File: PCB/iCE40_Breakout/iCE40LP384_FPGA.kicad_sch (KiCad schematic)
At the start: 31 parts, among them J1 Conn_01x08, J2 Conn_01x10, J3 Conn_01x10, Q1 L2N7002SLLT1G, SW1 KH-6X6X5H-STM, U1 ICE40LP384-SG32

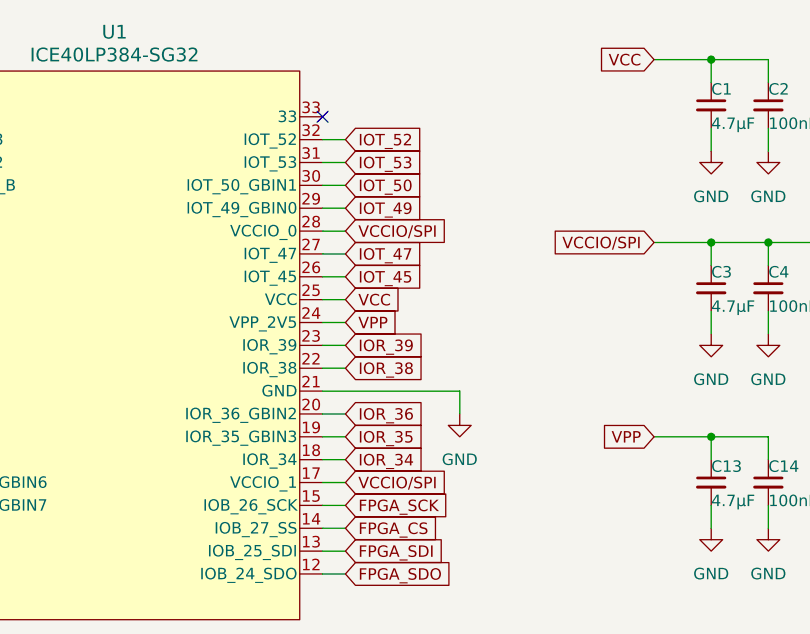
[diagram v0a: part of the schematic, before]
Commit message: Attached thermal pad to ground
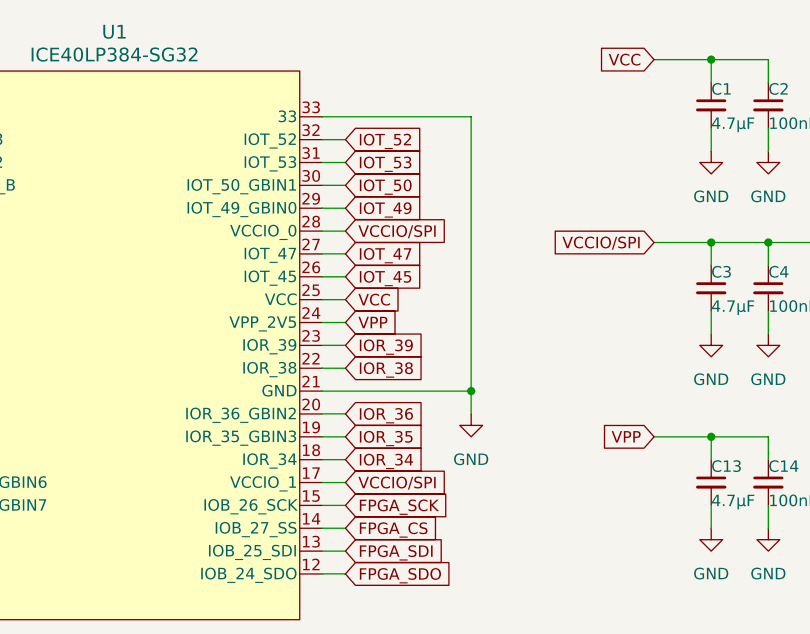
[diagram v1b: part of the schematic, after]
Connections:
- net GND: now also U1.33
- no-connect marks 1 -> 0
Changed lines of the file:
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@@
 	)
 	(junction
+		(at 123.19 60.96)
+		(diameter 0)
+		(color 0 0 0 0)
+	)
+	(junction
 		(at 215.9 44.45)
 		(diameter 0)
@@
 		(color 0 0 0 0)
 	)
-	(no_connect
-		(at 106.68 30.48)
-	)
 	(wire
 		(pts
@@
 	(wire
 		(pts
-			(xy 106.68 60.96) (xy 121.92 60.96)
+			(xy 106.68 60.96) (xy 123.19 60.96)
 		)
 		(stroke
@@
 	(wire
 		(pts
+			(xy 123.19 30.48) (xy 123.19 60.96)
+		)
+		(stroke
+			(width 0)
+			(type default)
+		)
+	)
+	(wire
+		(pts
 			(xy 248.92 143.51) (xy 255.27 143.51)
 		)
@@
 	(wire
 		(pts
-			(xy 121.92 60.96) (xy 121.92 63.5)
+			(xy 123.19 60.96) (xy 123.19 63.5)
 		)
 		(stroke
@@
 	(wire
 		(pts
+			(xy 106.68 30.48) (xy 123.19 30.48)
+		)
+		(stroke
+			(width 0)
+			(type default)
+		)
+	)
+	(wire
+		(pts
 			(xy 30.48 133.35) (xy 30.48 135.89)
 		)
@@
 	(symbol
 		(lib_id "power:GND")
-		(at 121.92 63.5 0)
+		(at 123.19 63.5 0)
 		(unit 1)
 		(exclude_from_sim no)
@@
 		(fields_autoplaced yes)
 		(property "Reference" "#PWR014"
-			(at 121.92 69.85 0)
+			(at 123.19 69.85 0)
 			(effects
 				(font
@@
 		)
 		(property "Value" "GND"
-			(at 121.92 68.58 0)
+			(at 123.19 68.58 0)
 			(effects
 				(font
@@
 		)
 		(property "Footprint" ""
-			(at 121.92 63.5 0)
+			(at 123.19 63.5 0)
 			(effects
 				(font
@@
 		)
 		(property "Datasheet" ""
-			(at 121.92 63.5 0)
+			(at 123.19 63.5 0)
 			(effects
 				(font
@@
 		)
 		(property "Description" "Power symbol creates a global label with name \"GND\" , ground"
-			(at 121.92 63.5 0)
+			(at 123.19 63.5 0)
 			(effects
 				(font
